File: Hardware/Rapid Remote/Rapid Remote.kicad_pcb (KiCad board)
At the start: 2 copper layers, 34.2 x 56.1 mm, 27 parts, among them U2 ESP32-C3-MINI-1-N4

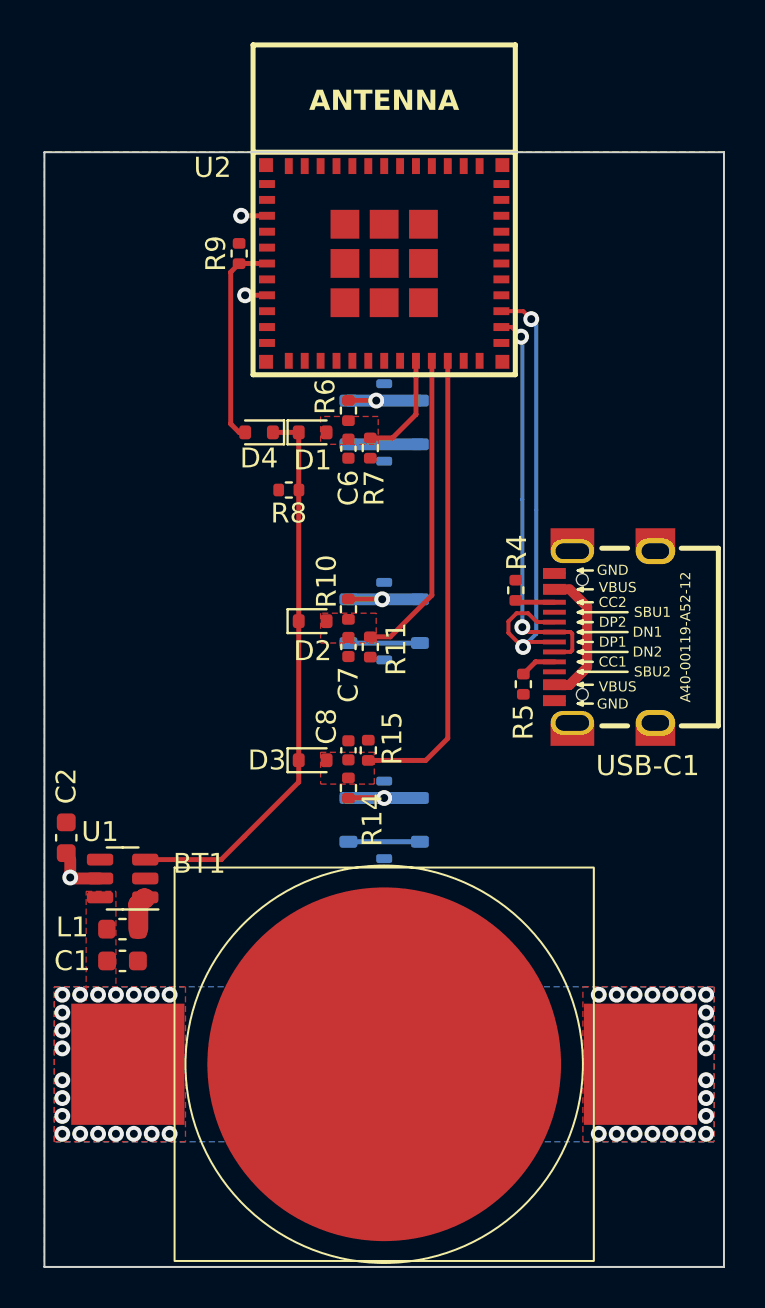
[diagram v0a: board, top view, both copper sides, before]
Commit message: updated remote to rev C
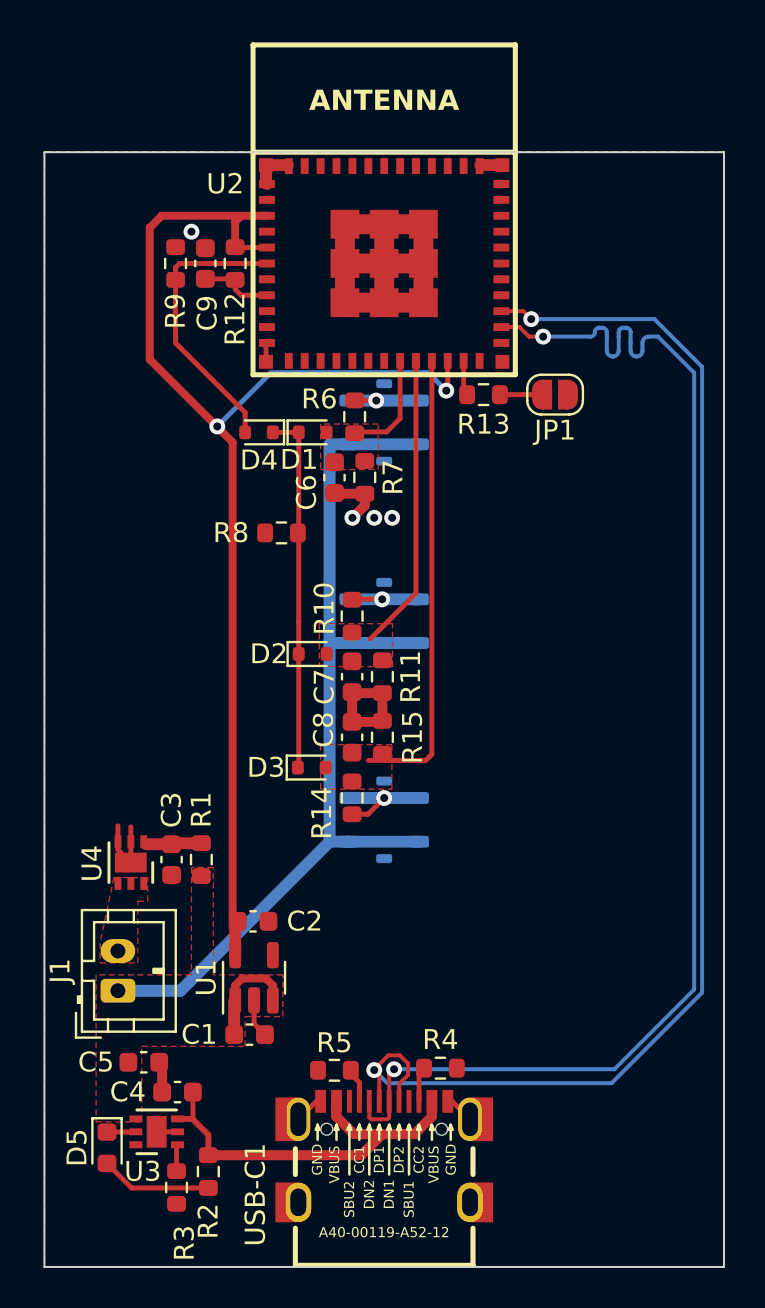
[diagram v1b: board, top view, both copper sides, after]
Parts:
- removed BT1: Battery_Cell, personal:MY-2032-04
- removed L1: 4.7u, Inductor_SMD:L_0603_1608Metric
- added C3: 100n, Capacitor_SMD:C_0603_1608Metric, F.Cu at (140.9, 104.2)
- added C4: 10u, Capacitor_SMD:C_0603_1608Metric, F.Cu at (141.2, 115.9)
- added C5: 1u, Capacitor_SMD:C_0603_1608Metric, F.Cu at (139.5, 114.4)
- added C9: 1u, Capacitor_SMD:C_0603_1608Metric, F.Cu at (142.6, 74.2)
- added D5: LED, LED_SMD:LED_0603_1608Metric, F.Cu at (137.7, 118.7)
- added J1: Conn_01x02_Socket, Connector_JST:JST_PH_B2B-PH-K_1x02_P2.00mm_Vertical, F.Cu at (138.2, 110.8)
- added JP1: SolderJumper_2_Open, Jumper:SolderJumper-2_P1.3mm_Open_RoundedPad1.0x1.5mm, F.Cu at (160.2, 80.8)
- added R1: 1k, Resistor_SMD:R_0603_1608Metric, F.Cu at (142.4, 104.2)
- added R12: 10k, Resistor_SMD:R_0603_1608Metric, F.Cu at (144.1, 74.2)
- added R13: 100R, Resistor_SMD:R_0603_1608Metric, F.Cu at (156.6, 80.8)
- added R2: 1k, Resistor_SMD:R_0603_1608Metric, F.Cu at (142.8, 119.9)
- added R3: 47.5k, Resistor_SMD:R_0603_1608Metric, F.Cu at (141.2, 120.7)
- added U3: WS4518D, Package_DFN_QFN:DFN-6-1EP_2x2mm_P0.65mm_EP1x1.6mm, F.Cu at (140.2, 117.9)
- added U4: XB6096I2SV, Package_DFN_QFN:DFN-6-1EP_2x2mm_P0.65mm_EP1x1.6mm, F.Cu at (138.8, 104.3)
- C1, C2: value 10u -> 1u
- C6, C7, C8: footprint Capacitor_SMD:C_0402_1005Metric -> Capacitor_SMD:C_0603_1608Metric
- R10, R11, R14, R15, R4, R5, R6, R7, R8, R9: footprint Resistor_SMD:R_0402_1005Metric -> Resistor_SMD:R_0603_1608Metric
- U1: value ~ -> MIC5504-3.3YM5; footprint Package_TO_SOT_SMD:SOT-23-6 -> Package_TO_SOT_SMD:SOT-23-5
- moved USB-C1 30.0 mm to (151.6, 120.3), turned to -90 degrees
- moved R4 24.3 mm to (154.4, 114.7), turned to 0 degrees
- moved R5 21.6 mm to (149.1, 114.8), turned to 180 degrees
- moved C2 10.3 mm to (145.0, 107.3), turned to 0 degrees
- moved U1 8.29 mm to (145.1, 110.1), turned to 90 degrees
- moved C1 7.39 mm to (144.8, 113.0)
- moved R9 3.24 mm to (141.1, 74.2)
- moved R8 2.19 mm to (146.4, 87.8)
- moved D2 1.65 mm to (148.0, 93.9)
- moved C6 1.62 mm to (149.1, 85.0)
- moved R11 1.62 mm to (151.5, 95.0)
- moved C7 1.51 mm to (150.0, 95.0)
- moved R7 1.50 mm to (150.6, 85.0)
- moved R15 0.97 mm to (151.5, 98.0)
- moved C8 0.68 mm to (150.0, 98.0)
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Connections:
- C1 pad 1: +3V0 -> +3V8
- U1 pad 1: Net-(U1-SW) -> +3V8
- U1 pad 3: EN_LDO -> +3V8
- U2 pad 19: unconnected-(U2-IO5/GPIO5/ADC2_CH0/FSPIWP/MTDI-Pad19) -> 8S
- U2 pad 20: 8S -> 6S
- U2 pad 21: 6S -> 4S
- U2 pad 22: 4S -> +3V3
- U2 pad 23: unconnected-(U2-IO9/GPIO9-Pad23) -> Net-(U2-IO9/GPIO9)
- U2 pad 5: unconnected-(U2-IO2/GPIO2/ADC1_CH2/FSPIQ-Pad5) -> +3V3
- U2 pad 8: +3V3 -> Net-(U2-EN)
- s4 pad P3: +3V3 -> +3V8
- s4 pad P4: +3V3 -> +3V8
- s6 pad P3: +3V3 -> +3V8
- s6 pad P4: +3V3 -> +3V8
- s8 pad P3: +3V3 -> +3V8
- s8 pad P4: +3V3 -> +3V8
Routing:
- net +3V8: track 0.00 -> 52.9 mm
- net GND: track 0.00 -> 48.7 mm, vias 0 -> 4
- net USB_D-: track 20.2 -> 67.4 mm
- net +3V3: track 15.6 -> 62.5 mm, vias 3 -> 2
- net USB_D+: track 24.5 -> 67.4 mm
- net +5V: track 7.39 -> 20.9 mm
- net EN_LDO: track 28.2 -> 17.8 mm
- net Net-(D5-A): track 0.00 -> 5.61 mm
- net LATCH: track 10.5 -> 14.4 mm
- net Net-(U2-EN): track 0.00 -> 3.72 mm
- net Net-(U4-VDD): track 0.00 -> 2.97 mm
- net Net-(JP1-B): track 0.00 -> 1.93 mm
- net Net-(U2-IO9/GPIO9): track 0.00 -> 1.86 mm
- net Net-(U1-SW): track 1.72 -> 0.00 mm
- net Net-(D5-K): track 0.00 -> 1.46 mm
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- added copper zone on F.Cu, net +3V8
- added copper zone on B.Cu, net GND
- added copper zone on F.Cu, net Net-(J1-Pin_2)
- removed copper zone on B.Cu, net +3V0
- removed copper zone on F.Cu, net +3V0
- removed copper zone on B.Cu, net +3V3
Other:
- board text added: "Rapid Training Box Remote © 2023 Thomas Whyte-Venables Rev. C"
- board text removed: "Rapid Training Box Remote © 2023 Thomas Whyte-Venables Rev. B"

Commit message: added bom and pos files
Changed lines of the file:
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@@
     (fp_line (start 3.95 2.8) (end 3.95 -1.7)
       (stroke (width 0.1) (type solid)) (layer "F.Fab"))
-    (pad "1" thru_hole roundrect (at 0 0 90) (size 1.2 1.75) (drill 0.75) (layers "*.Cu" "*.Mask") (roundrect_rratio 0.208333)
+    (pad "1" thru_hole roundrect (at 0 0 90) (size 1.2 1.75) (drill 0.75) (layers "*.Cu" "*.Mask") (roundrect_rratio 0.2083333333)
       (net 40 "+3V8") (pinfunction "Pin_1") (pintype "passive"))
     (pad "2" thru_hole oval (at 2 0 90) (size 1.2 1.75) (drill 0.75) (layers "*.Cu" "*.Mask")

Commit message: rev c of remote and cad
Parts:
- added H1: MountingHole, MountingHole:MountingHole_3.2mm_M3, F.Cu at (165.2, 66.6)
- added H2: MountingHole, MountingHole:MountingHole_3.2mm_M3, F.Cu at (138.0, 93.9)
- added H3: MountingHole, MountingHole:MountingHole_3.2mm_M3, F.Cu at (165.2, 121.2)
- J1: footprint Connector_JST:JST_PH_B2B-PH-K_1x02_P2.00mm_Vertical -> Connector_JST:JST_PH_S2B-PH-SM4-TB_1x02-1MP_P2.00mm_Horizontal
- moved C1 6.32 mm to (150.4, 110.1)
- moved C2 6.32 mm to (150.6, 104.4)
- moved U1 6.32 mm to (150.7, 107.2)
- moved J1 4.14 mm to (141.9, 109.0)
- moved C3 1.75 mm to (140.8, 102.5)
- moved R1 1.75 mm to (142.3, 102.5)
- moved U4 1.75 mm to (138.8, 102.6)
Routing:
- net +3V8: track 52.9 -> 58.7 mm, vias 0 -> 3
- net +3V3: track 62.5 -> 63.3 mm
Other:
- board size 34.2 x 56.1 mm -> 34.2 x 61.6 mm

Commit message: updated gpio values
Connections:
- U1 pad 3: +3V8 -> EN_LDO
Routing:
- net EN_LDO: track 17.8 -> 29.0 mm
- net +3V8: track 58.7 -> 55.0 mm
- net GND: vias 4 -> 7
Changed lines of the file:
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@@
       (net 2 "GND") (pinfunction "GND") (pintype "power_in"))
     (pad "3" smd roundrect (at -1.1375 0.95 90) (size 1.325 0.6) (layers "F.Cu" "F.Paste" "F.Mask") (roundrect_rratio 0.25)
-      (net 40 "+3V8") (pinfunction "EN") (pintype "input"))
+      (net 3 "EN_LDO") (pinfunction "EN") (pintype "input"))
     (pad "4" smd roundrect (at 1.1375 0.95 90) (size 1.325 0.6) (layers "F.Cu" "F.Paste" "F.Mask") (roundrect_rratio 0.25)
       (net 39 "unconnected-(U1-NC-Pad4)") (pinfunction "NC") (pintype "no_connect"))
@@
   (segment (start 148.182 116.368) (end 147.28 117.27) (width 0.25) (layer "F.Cu") (net 2))
   (segment (start 138.15 101.55) (end 138.15 101.95) (width 0.25) (layer "F.Cu") (net 2))
+  (via (at 153 97.5) (size 0.8) (drill 0.4) (layers "F.Cu" "B.Cu") (free) (net 2))
   (via (at 141.9 72.6) (size 0.8) (drill 0.4) (layers "F.Cu" "B.Cu") (free) (net 2))
   (via (at 150 87) (size 0.8) (drill 0.4) (layers "F.Cu" "B.Cu") (net 2))
+  (via (at 153 94.6) (size 0.8) (drill 0.4) (layers "F.Cu" "B.Cu") (free) (net 2))
   (via (at 152 87) (size 0.8) (drill 0.4) (layers "F.Cu" "B.Cu") (free) (net 2))
   (via (at 151.1 87) (size 0.8) (drill 0.4) (layers "F.Cu" "B.Cu") (free) (net 2))
+  (via (at 153 95.9) (size 0.8) (drill 0.4) (layers "F.Cu" "B.Cu") (free) (net 2))
+  (segment (start 150.6 103.897183) (end 150.6 106.6) (width 0.25) (layer "F.Cu") (net 3))
+  (segment (start 151.6 107.6) (end 151.6 108.35) (width 0.25) (layer "F.Cu") (net 3))
   (segment (start 147.3 82.7) (end 146 82.7) (width 0.25) (layer "F.Cu") (net 3))
+  (segment (start 150.6 106.6) (end 151.6 107.6) (width 0.25) (layer "F.Cu") (net 3))
+  (segment (start 147.255 99.568) (end 147.255 101.655) (width 0.25) (layer "F.Cu") (net 3))
   (segment (start 147.3 99.2) (end 147.3 92.2) (width 0.25) (layer "F.Cu") (net 3))
+  (segment (start 148.6 103) (end 149.702817 103) (width 0.25) (layer "F.Cu") (net 3))
   (segment (start 147.3 82.7) (end 147.3 92.2) (width 0.25) (layer "F.Cu") (net 3))
+  (segment (start 147.255 101.655) (end 148.6 103) (width 0.25) (layer "F.Cu") (net 3))
+  (segment (start 149.702817 103) (end 150.6 103.897183) (width 0.25) (layer "F.Cu") (net 3))
   (segment (start 152.4 79.1) (end 152.4 82) (width 0.25) (layer "F.Cu") (net 4))
   (segment (start 150.177 82.677) (end 150.114 82.74) (width 0.25) (layer "F.Cu") (net 4))
@@
   (segment (start 149.7 108.35) (end 149.7 110.025) (width 0.4) (layer "F.Cu") (net 40))
   (segment (start 137.85 110.8) (end 138.2 110.8) (width 0.6) (layer "F.Cu") (net 40))
-  (segment (start 151.6 107.6) (end 151.25 107.25) (width 0.4) (layer "F.Cu") (net 40))
-  (segment (start 150.05 107.25) (end 149.7 107.6) (width 0.4) (layer "F.Cu") (net 40))
-  (segment (start 151.6 108.35) (end 151.6 107.6) (width 0.4) (layer "F.Cu") (net 40))
   (segment (start 139.9 110.8) (end 139.05 109.95) (width 0.6) (layer "F.Cu") (net 40))
   (segment (start 148.625 110.075) (end 148.6 110.05) (width 0.4) (layer "F.Cu") (net 40))
   (segment (start 138.2 110.8) (end 139.05 109.95) (width 0.6) (layer "F.Cu") (net 40))
-  (segment (start 151.25 107.25) (end 150.05 107.25) (width 0.4) (layer "F.Cu") (net 40))
   (segment (start 139.05 110.75) (end 139.1 110.8) (width 0.25) (layer "F.Cu") (net 40))
-  (segment (start 149.7 107.6) (end 149.7 108.35) (width 0.4) (layer "F.Cu") (net 40))
   (segment (start 149.65 110.075) (end 148.625 110.075) (width 0.4) (layer "F.Cu") (net 40))
   (segment (start 139.05 109.95) (end 139.05 110.75) (width 1) (layer "F.Cu") (net 40))

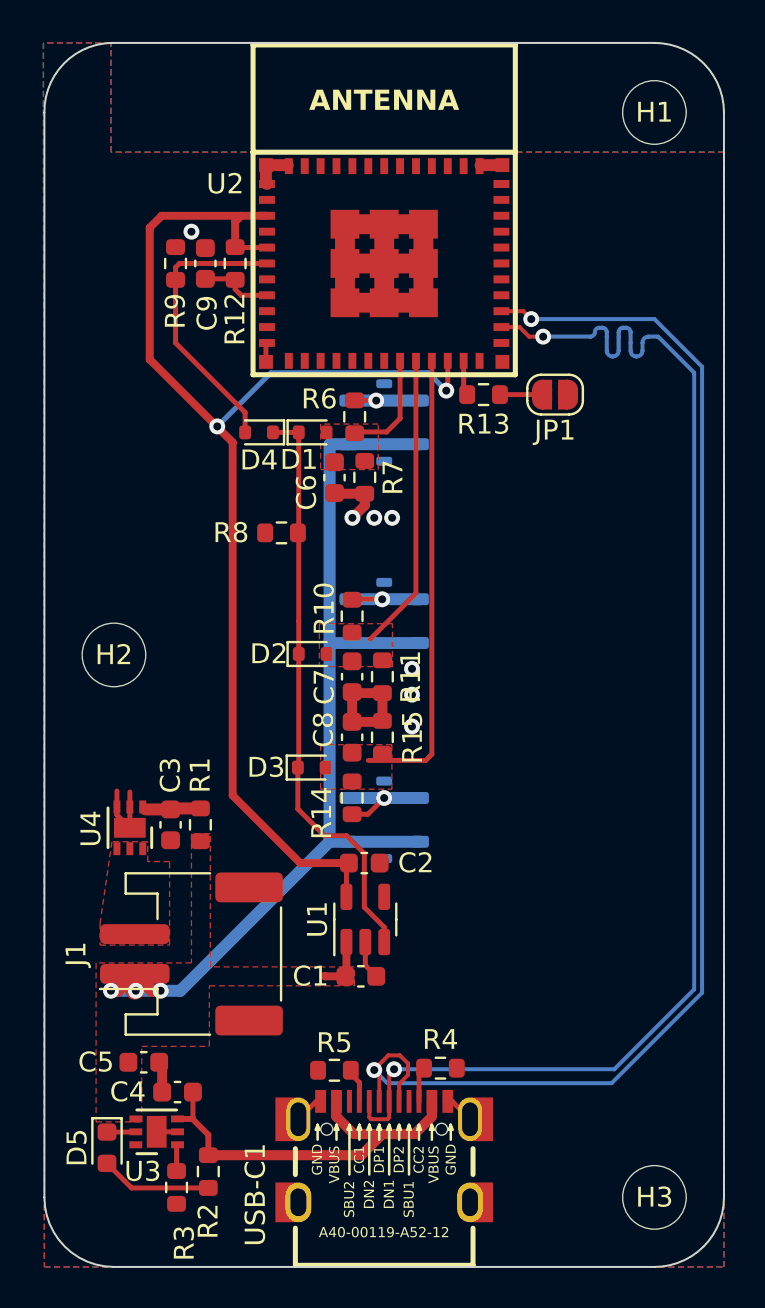
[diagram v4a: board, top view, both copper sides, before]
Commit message: added boot and reset buttons
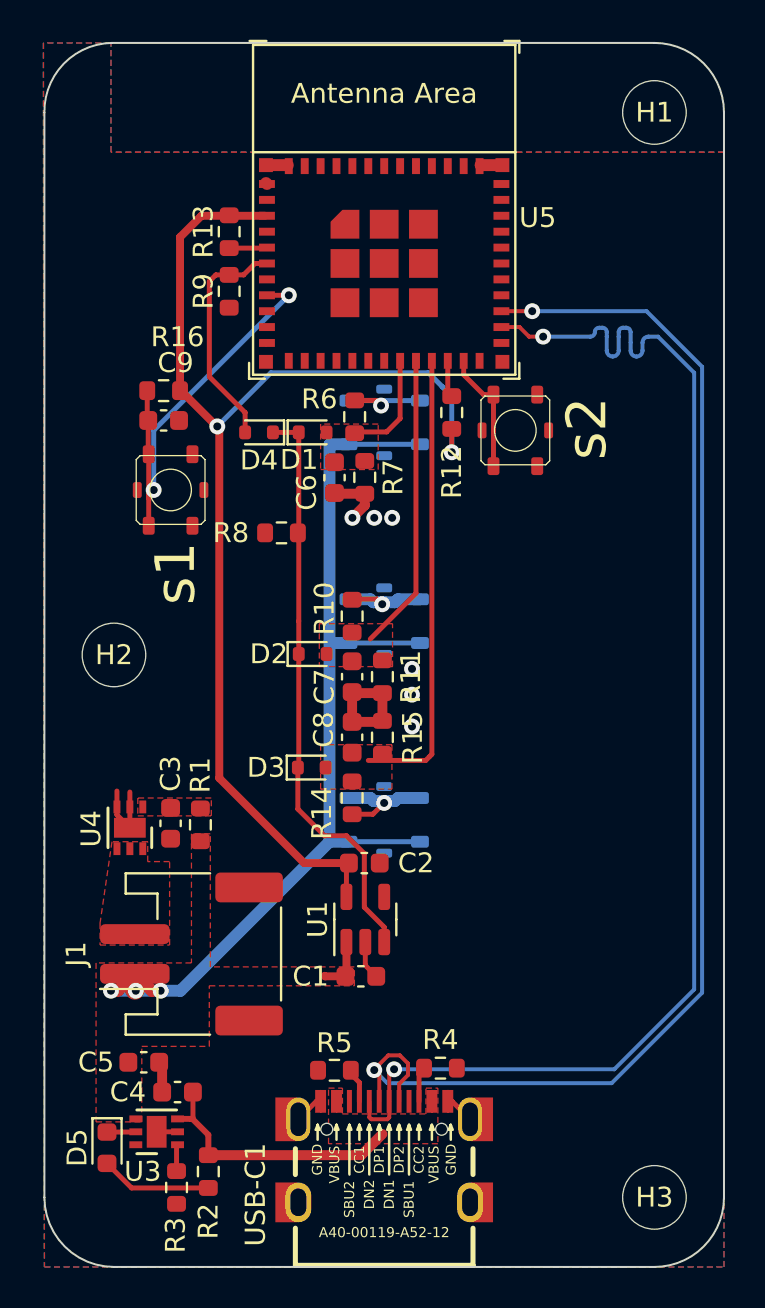
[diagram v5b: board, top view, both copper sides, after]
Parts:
- removed JP1: SolderJumper_2_Open, Jumper:SolderJumper-2_P1.3mm_Open_RoundedPad1.0x1.5mm
- removed U2: ESP32-C3-MINI-1-N4, Personal:ESP32-­C3-­MINI­-1
- added R16: 10k, Resistor_SMD:R_0603_1608Metric, F.Cu at (140.5, 80.6)
- added U5: ESP32-C3-MINI-1, PCM_Espressif:ESP32-C3-MINI-1, F.Cu at (151.6, 71.5)
- added s1: BUTTON_4PIN_TS_1177, rapidtraining:TS-1177-C-B-B, F.Cu at (140.8, 85.6)
- added s2: BUTTON_4PIN_TS_1177, rapidtraining:TS-1177-C-B-B, F.Cu at (158.2, 82.6)
- R13: value 100R -> 10k
- s4, s6, s8: footprint Personal:TS-1177-C-B-B -> rapidtraining:TS-1177-C-B-B
- moved R13 15.2 mm to (143.8, 72.6), turned to 90 degrees
- moved R12 13.2 mm to (155.0, 81.7), turned to 90 degrees
- moved C9 8.17 mm to (140.5, 82.1), turned to 0 degrees
- moved R9 3.04 mm to (143.8, 75.6), turned to -90 degrees
- moved C3 0.08 mm to (140.8, 102.4)
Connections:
- C9 pad 1: Net-(U2-EN) -> Net-(U5-EN/CHIP_PU)
- R12 pad 2: Net-(U2-EN) -> Net-(U5-GPIO8)
- R13 pad 2: Net-(JP1-B) -> +3V3
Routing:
- net GND: track 48.7 -> 23.2 mm, vias 7 -> 6
- net Net-(U5-EN/CHIP_PU): track 0.00 -> 21.1 mm, vias 0 -> 2
- net +5V: track 20.9 -> 13.7 mm
- net Net-(U5-GPIO9): track 0.00 -> 6.21 mm
- net Net-(U2-EN): track 3.72 -> 0.00 mm
- net Net-(U4-VDD): track 2.97 -> 0.14 mm
- net LATCH: track 14.4 -> 11.6 mm
- net +3V3: track 63.3 -> 60.5 mm
- net Net-(JP1-B): track 1.93 -> 0.00 mm
- net Net-(U5-GPIO8): track 0.00 -> 1.86 mm
- added copper zone on F.Cu, net +5V
- added copper zone on F.Cu, net Net-(U4-VDD)
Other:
- board text added: "Rapid Training Box Remote © 2023 Thomas Whyte-Venables Rev. D"
- board text removed: "Rapid Training Box Remote © 2023 Thomas Whyte-Venables Rev. C"
